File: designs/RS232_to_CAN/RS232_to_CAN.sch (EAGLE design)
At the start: 53 parts, among them IC1 STM32F042K6T6TR, IC2 TJA1050T_CM,118, IC3 MAX232DRG4, IC4 FT232RL-TUBE, J1 FTSH-107-01-L-DV-K-A, J2 K202XHT-E9S-N, J3 K202XHT-E9S-N, J4 PJ-002AH-SMT-TR, J5 10118192-0001LF, Q1 FDN5632N-F085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

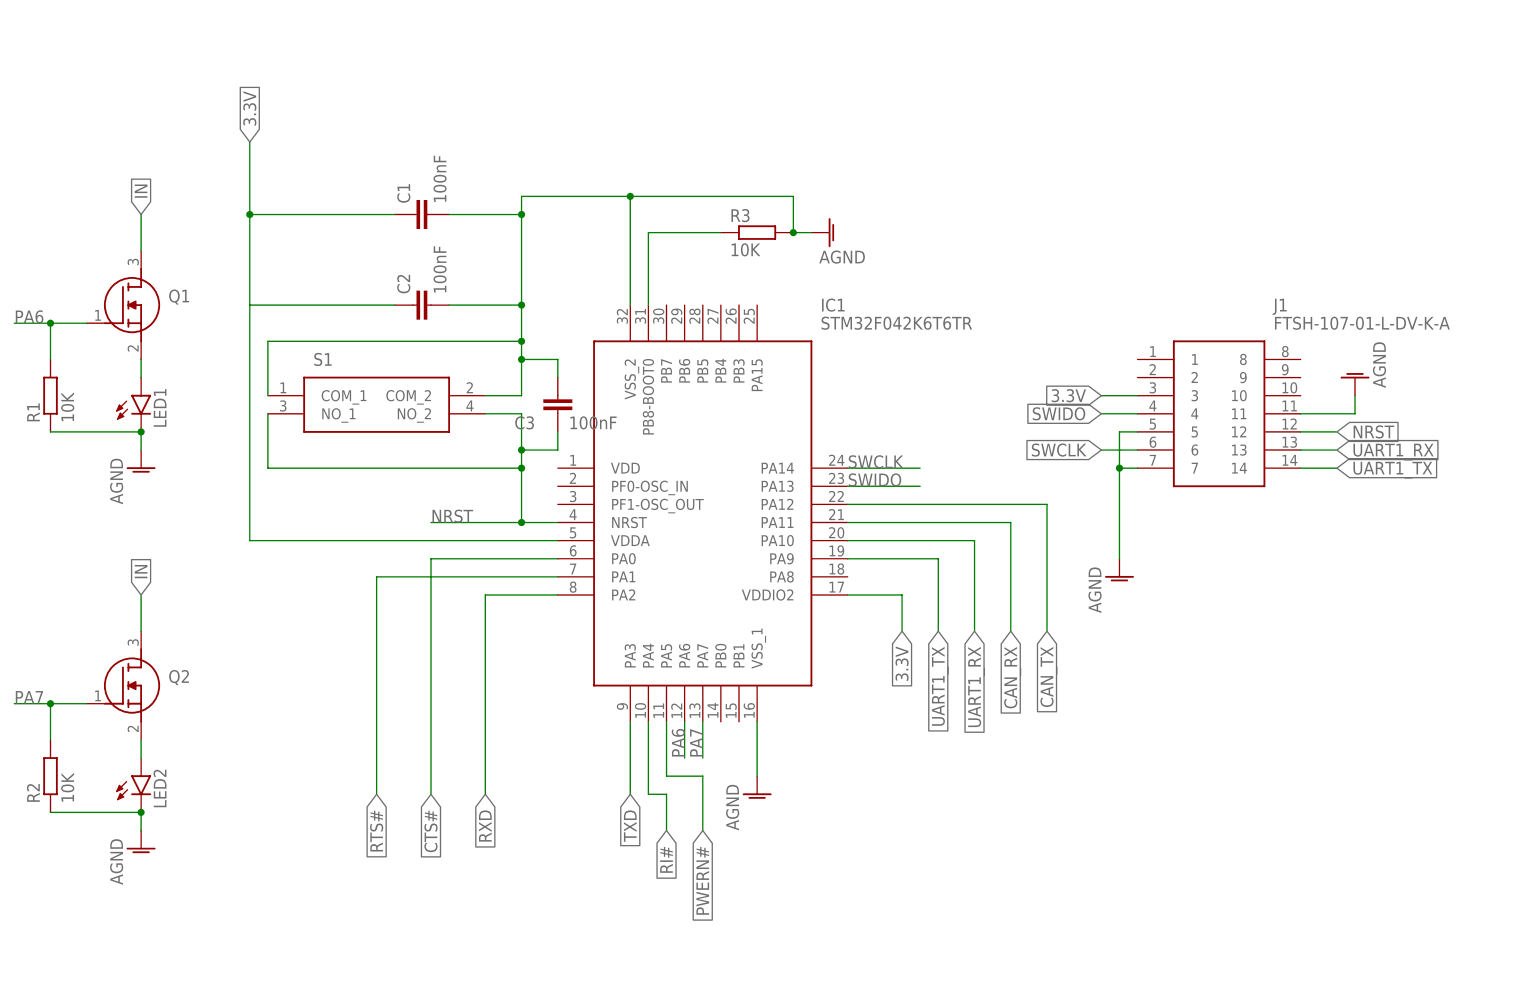
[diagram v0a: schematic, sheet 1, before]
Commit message: added brd laxout
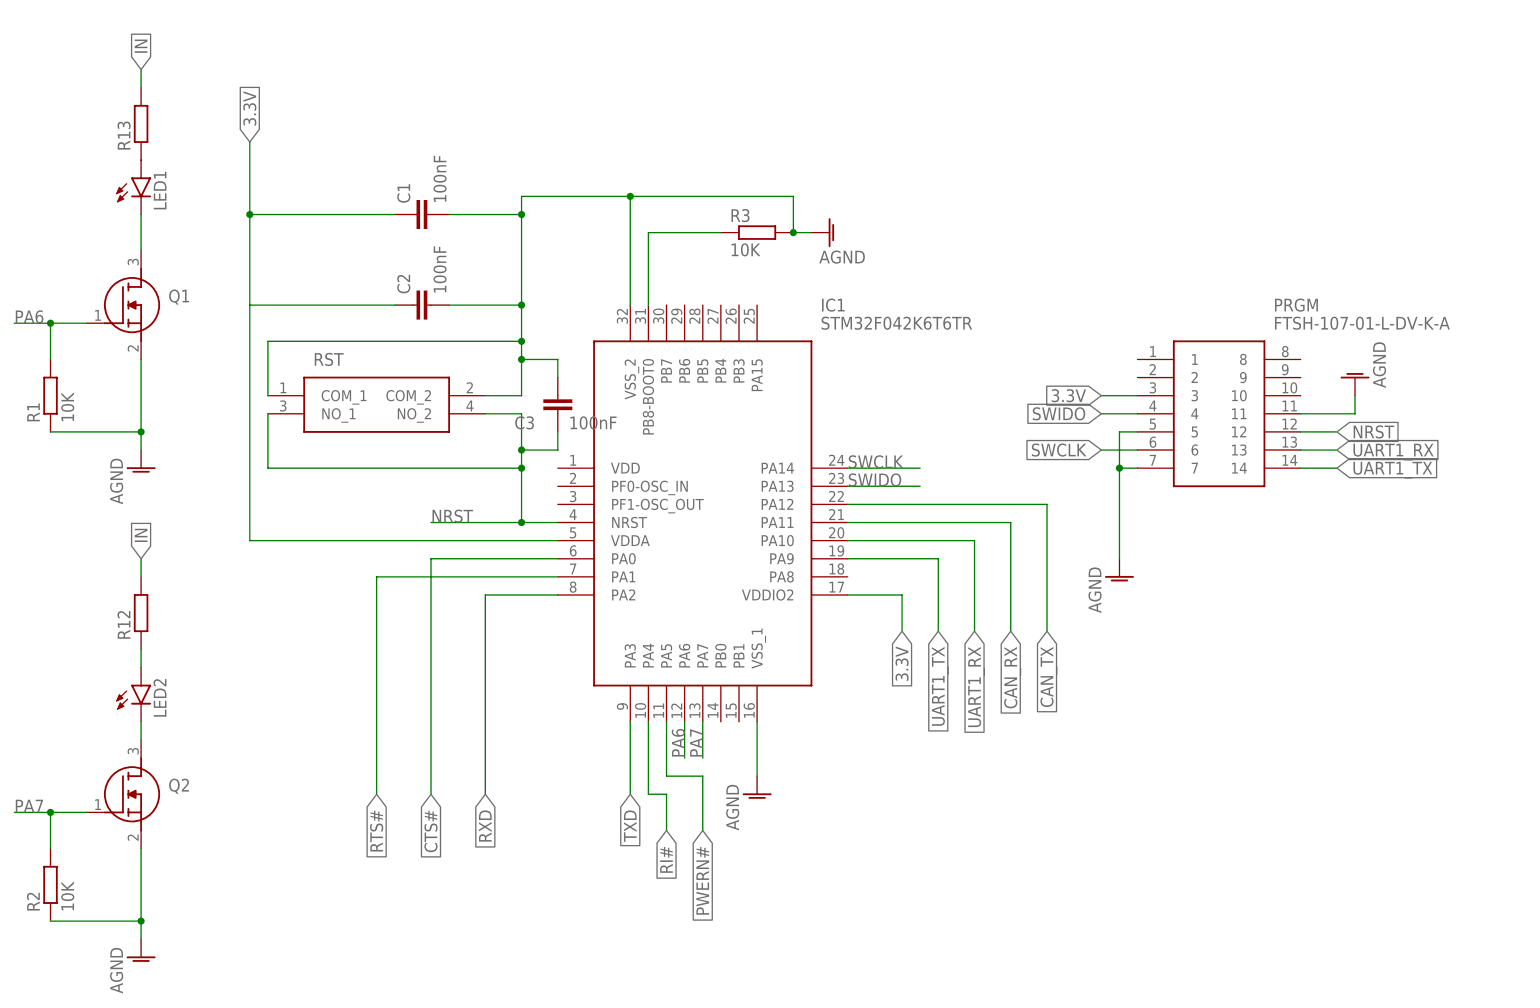
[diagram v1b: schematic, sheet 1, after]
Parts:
- added R12, R13: (no value), CommonParts:R-EU_805R0805
- renumbered J1 to PRGM, S1 to RST
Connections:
- new net N$22: R12.2
- new net N$23: R13.2
- net 5V: no longer J4.1_1, J4.1_2
- net AGND: now also Q1.S, Q2.S; no longer LED1.C, LED2.C
- net IN: now also J4.1_1, J4.1_2, LED1.C, LED2.C
- net N$13: now also R12.1; no longer Q2.S
- net N$8: now also R13.1; no longer Q1.S
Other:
- moved on the sheet: LED1, LED2, Q2, R2
